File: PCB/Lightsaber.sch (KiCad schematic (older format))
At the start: 28 parts, among them Q1 SS8050, Q2 SS8050, Q3 SS8050, Q4 8205A, SW1 SW_Push, U1 DW01A

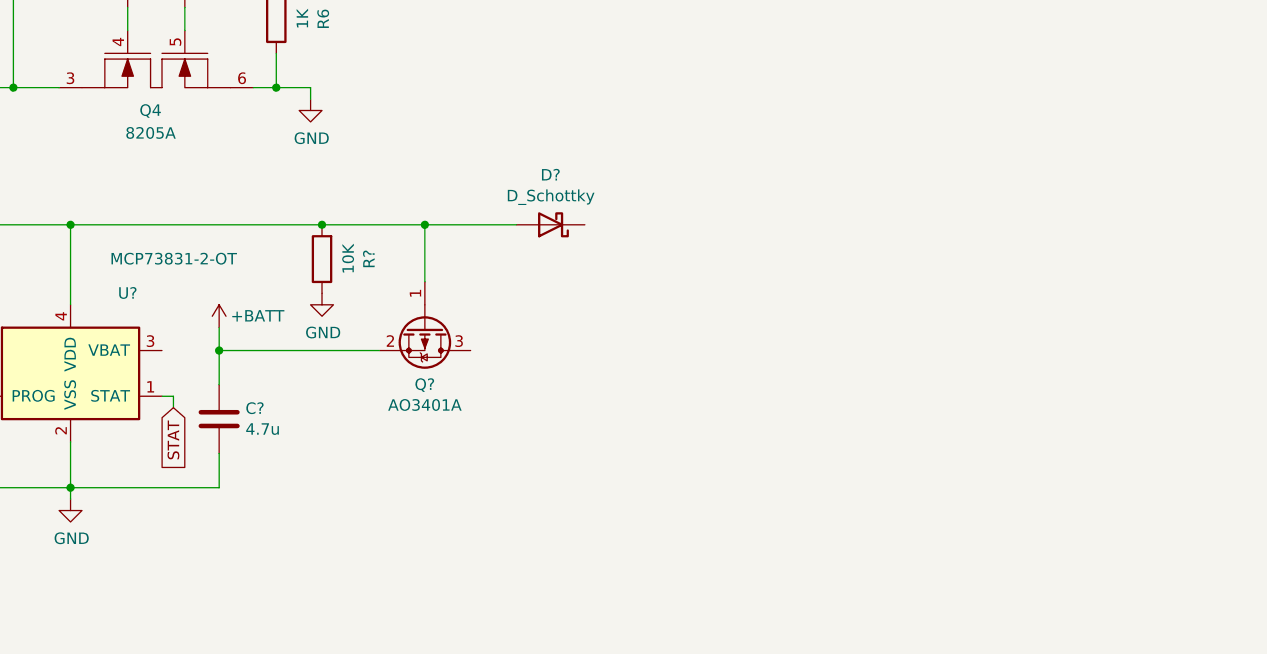
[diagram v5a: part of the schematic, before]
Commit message: boost converter added
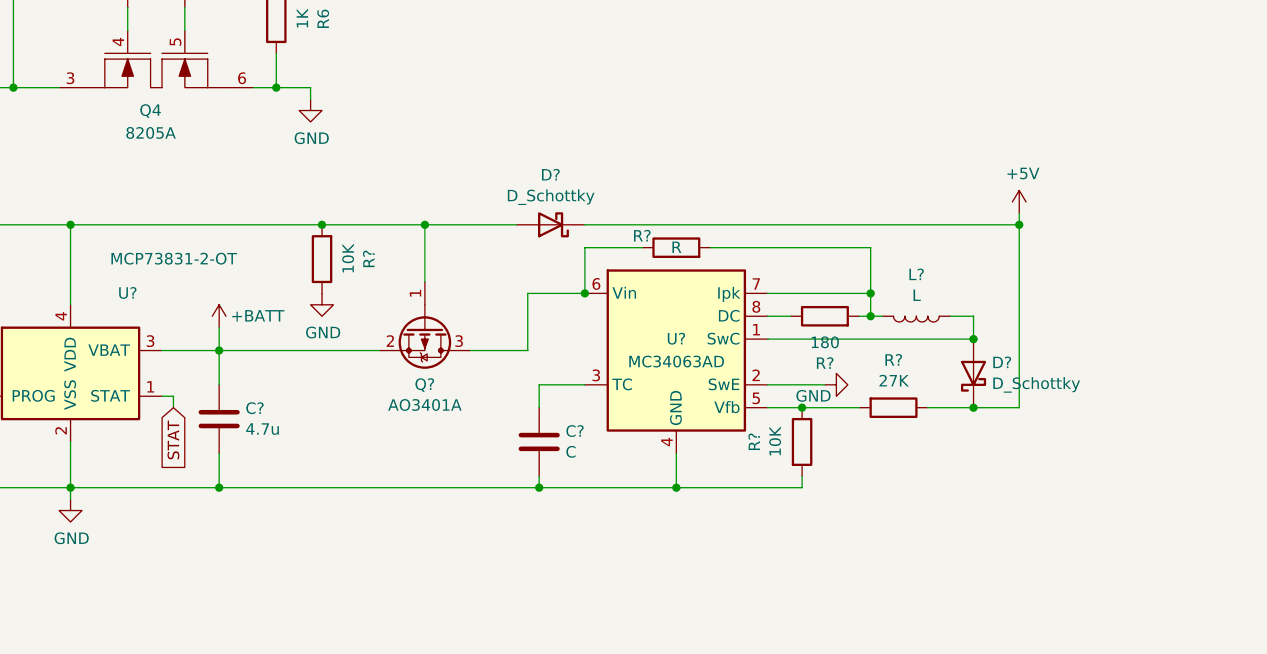
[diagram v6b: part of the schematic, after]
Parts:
- added C?: C, symbol Device:C
- added D?: D_Schottky, symbol Device:D_Schottky
- added L?: L, symbol Device:L
- added R?: 180, Resistor_SMD:R_0402_1005Metric, symbol Device:R
- added R?: R, Resistor_SMD:R_0402_1005Metric, symbol Device:R
- added R?: 10K, Resistor_SMD:R_0402_1005Metric, symbol Device:R
- added R?: 27K, Resistor_SMD:R_0402_1005Metric, symbol Device:R
- added U?: MC34063AD, Package_SO:SOIC-8_3.9x4.9mm_P1.27mm, symbol Regulator_Switching:MC34063AD
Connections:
- net +5V: now also D?.1 (K), D?.1 (K), R?.1
- net +BATT: now also U?.3 (VBAT)
- net GND: now also C?.2, R?.2, U?.2 (SwE), U?.4 (GND)
- net at Q?.3 (D): now also R?.1, U?.6 (Vin)
- new net: D?.2 (A), L?.1, U?.1 (SwC)
- new net: C?.1, U?.3 (TC)
- new net: R?.1, R?.2, U?.5 (Vfb)
- new net: L?.2, R?.2, R?.2, U?.7 (Ipk)
- new net: R?.1, U?.8 (DC)
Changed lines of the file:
@@
 Connection ~ 2600 2750
 Connection ~ 3700 2750
+$Comp
+L Regulator_Switching:MC34063AD U?
+U 1 1 632360AA
+P 5250 3250
+F 0 "U?" H 5250 3250 50  0000 C CNN
+F 1 "MC34063AD" H 5250 3150 50  0000 C CNN
+F 2 "Package_SO:SOIC-8_3.9x4.9mm_P1.27mm" H 5300 2800 50  0001 L CNN
+F 3 "http://www.onsemi.com/pub_link/Collateral/MC34063A-D.PDF" H 5750 3150 50  0001 C CNN
+	1    5250 3250
+	1    0    0    -1
+$EndComp
+Wire Wire Line
+	4850 3050 4600 3050
+Wire Wire Line
+	4600 3050 4600 3300
+Wire Wire Line
+	4600 3300 4350 3300
+$Comp
+L Device:R R?
+U 1 1 6324142B
+P 5900 3150
+F 0 "R?" V 5693 3150 50  0000 C CNN
+F 1 "180" V 5784 3150 50  0000 C CNN
+F 2 "Resistor_SMD:R_0402_1005Metric" V 5830 3150 50  0001 C CNN
+F 3 "~" H 5900 3150 50  0001 C CNN
+	1    5900 3150
+	0    -1   -1   0
+$EndComp
+$Comp
+L Device:L L?
+U 1 1 63241E87
+P 6300 3150
+F 0 "L?" V 6119 3150 50  0000 C CNN
+F 1 "L" V 6210 3150 50  0000 C CNN
+F 2 "" H 6300 3150 50  0001 C CNN
+F 3 "~" H 6300 3150 50  0001 C CNN
+	1    6300 3150
+	0    1    1    0
+$EndComp
+Wire Wire Line
+	5650 3250 6550 3250
+Wire Wire Line
+	6550 3250 6550 3150
+Wire Wire Line
+	6550 3150 6450 3150
+Wire Wire Line
+	6150 3150 6100 3150
+Wire Wire Line
+	5750 3150 5650 3150
+Wire Wire Line
+	5250 3750 5250 3900
+Wire Wire Line
+	6100 3150 6100 3050
+Wire Wire Line
+	6100 3050 5650 3050
+Connection ~ 6100 3150
+Wire Wire Line
+	6100 3150 6050 3150
+$Comp
+L Device:R R?
+U 1 1 63252DB4
+P 5250 2850
+F 0 "R?" V 5300 3000 50  0000 C CNN
+F 1 "R" V 5250 2850 50  0000 C CNN
+F 2 "Resistor_SMD:R_0402_1005Metric" V 5180 2850 50  0001 C CNN
+F 3 "~" H 5250 2850 50  0001 C CNN
+	1    5250 2850
+	0    -1   -1   0
+$EndComp
+Wire Wire Line
+	6100 3050 6100 2850
+Wire Wire Line
+	6100 2850 5400 2850
+Connection ~ 6100 3050
+Wire Wire Line
+	5100 2850 4850 2850
+Wire Wire Line
+	4850 2850 4850 3050
+Connection ~ 4850 3050
+$Comp
+L Device:C C?
+U 1 1 632593ED
+P 4650 3700
+F 0 "C?" H 4765 3746 50  0000 L CNN
+F 1 "C" H 4765 3655 50  0000 L CNN
+F 2 "" H 4688 3550 50  0001 C CNN
+F 3 "~" H 4650 3700 50  0001 C CNN
+	1    4650 3700
+	1    0    0    -1
+$EndComp
+Connection ~ 5250 3900
+Wire Wire Line
+	4850 3450 4650 3450
+Wire Wire Line
+	4650 3450 4650 3550
+Wire Wire Line
+	5250 3900 4650 3900
+Wire Wire Line
+	4650 3900 4650 3850
+$Comp
+L Device:R R?
+U 1 1 6326F515
+P 5800 3700
+F 0 "R?" V 5593 3700 50  0000 C CNN
+F 1 "10K" V 5684 3700 50  0000 C CNN
+F 2 "Resistor_SMD:R_0402_1005Metric" V 5730 3700 50  0001 C CNN
+F 3 "~" H 5800 3700 50  0001 C CNN
+	1    5800 3700
+	1    0    0    -1
+$EndComp
+$Comp
+L power:GND #PWR?
+U 1 1 6327EA47
+P 5900 3450
+F 0 "#PWR?" H 5900 3200 50  0001 C CNN
+F 1 "GND" V 5850 3500 50  0000 C CNN
+F 2 "" H 5900 3450 50  0001 C CNN
+F 3 "" H 5900 3450 50  0001 C CNN
+	1    5900 3450
+	0    -1   -1   0
+$EndComp
+Wire Wire Line
+	5900 3450 5650 3450
+Wire Wire Line
+	5650 3550 5800 3550
+Wire Wire Line
+	5800 3850 5800 3900
+Wire Wire Line
+	5800 3900 5250 3900
+$Comp
+L Device:R R?
+U 1 1 632885DC
+P 6200 3550
+F 0 "R?" V 5993 3550 50  0000 C CNN
+F 1 "27K" V 6084 3550 50  0000 C CNN
+F 2 "Resistor_SMD:R_0402_1005Metric" V 6130 3550 50  0001 C CNN
+F 3 "~" H 6200 3550 50  0001 C CNN
+	1    6200 3550
+	0    1    1    0
+$EndComp
+Wire Wire Line
+	6050 3550 5800 3550
+Connection ~ 5800 3550
+$Comp
+L Device:D_Schottky D?
+U 1 1 6328C7F1
+P 6550 3400
+F 0 "D?" V 6596 3320 50  0000 R CNN
+F 1 "D_Schottky" V 6505 3320 50  0000 R CNN
+F 2 "" H 6550 3400 50  0001 C CNN
+F 3 "~" H 6550 3400 50  0001 C CNN
+	1    6550 3400
+	0    -1   -1   0
+$EndComp
+Connection ~ 6550 3250
+Wire Wire Line
+	6550 3550 6350 3550
+Wire Wire Line
+	4650 3900 3250 3900
+Connection ~ 4650 3900
+Connection ~ 3250 3900
+Wire Wire Line
+	6550 3550 6750 3550
+Wire Wire Line
+	6750 3550 6750 2750
+Connection ~ 6550 3550
+$Comp
+L power:+5V #PWR?
+U 1 1 63297A5F
+P 6750 2700
+F 0 "#PWR?" H 6750 2550 50  0001 C CNN
+F 1 "+5V" H 6765 2873 50  0000 C CNN
+F 2 "" H 6750 2700 50  0001 C CNN
+F 3 "" H 6750 2700 50  0001 C CNN
+	1    6750 2700
+	1    0    0    -1
+$EndComp
+Wire Wire Line
+	4850 2750 6750 2750
+Connection ~ 6750 2750
+Wire Wire Line
+	6750 2750 6750 2700
+Wire Wire Line
+	3250 3300 3000 3300
 $EndSCHEMATC
